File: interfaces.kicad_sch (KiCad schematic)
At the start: 126 parts, among them J6001 HDMI-A_WE_685119134923, J6002 USB-C_USB4105-GF-A, J6003 MicroSD_693071020811, Q6001 BSS138PW, Q6002 BSS138PW, Q6003 BSS138PW, Q6004 BSS138PW, Q6005 BSS138PW, Q6006 BSS138PW, Q6007 BSS138PW, Q6008 BSS138PW, SW6001 SW_KMR211NGLFS_SMD, U6001 FT4232H_VQFN, U6002 NCP718BSN330T1G, U6003 TXU0304BQAR, U6004 TPD4E05U06QDQARQ1, U6005 SN74HC595B, U6006 TPD4E05U06QDQARQ1, U6007 TPD4E05U06QDQARQ1, U6008 TXU0304BQAR, U6009 TPD4E05U06QDQARQ1, U6010 TPD4E05U06QDQARQ1, Y6001 Oscillator_SMD_12MHz_KX-7

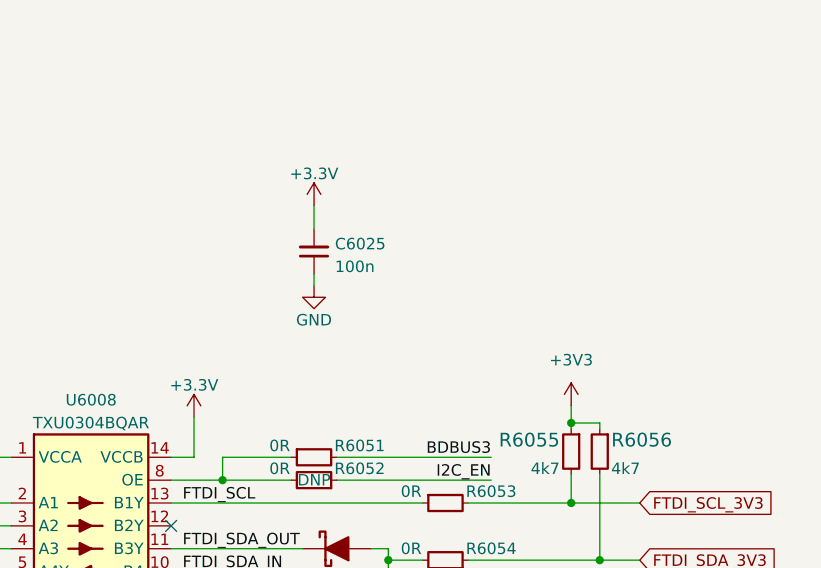
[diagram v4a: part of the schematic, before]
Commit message: Finish reworking power I2C and SPI termination
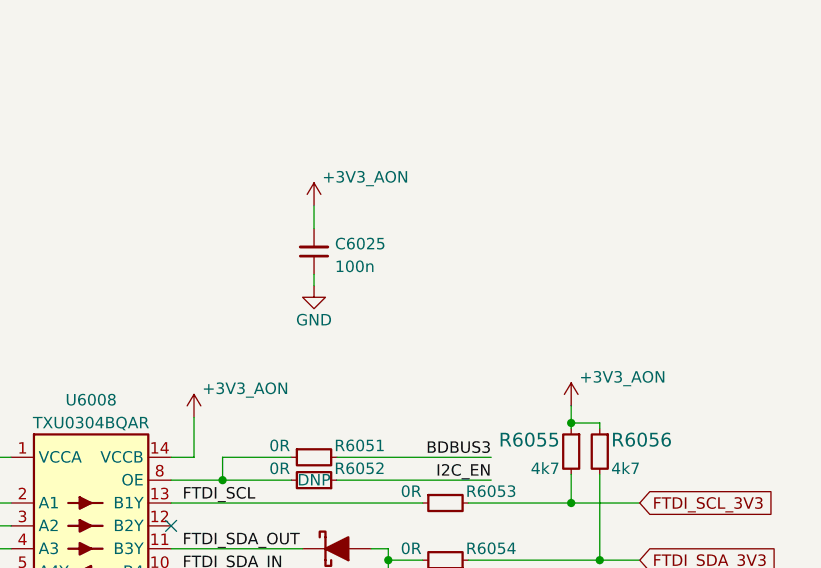
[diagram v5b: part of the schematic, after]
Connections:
- net +3V3: no longer C6025.2, R6055.1, R6056.1, U6008.14 (VCCB)
- new net +3V3_AON: C6025.2, R6055.1, R6056.1, U6008.14 (VCCB)
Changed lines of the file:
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@@
-    (pin "1")
-  )
-  (symbol (lib_id "antmicropower:+3.3V") (at 403.86 338.455 0) (unit 1)
-    (in_bom yes) (on_board yes)
-    (property "Reference" "#PWR0260" (id 0) (at 403.86 342.265 0)
-      (effects (font (size 1.27 1.27)) hide)
-    )
-    (property "Value" "+3.3V" (id 1) (at 403.86 334.899 0))
-    (property "Footprint" "" (id 2) (at 403.86 338.455 0)
-      (effects (font (size 1.27 1.27)) hide)
-    )
-    (property "Datasheet" "" (id 3) (at 403.86 338.455 0)
-      (effects (font (size 1.27 1.27)) hide)
-    )
     (pin "1")
   )
@@
     (pin "1")
     (pin "2")
+  )
+  (symbol (lib_id "sodimm-ddr5-tester:+3V3_AON") (at 417.195 314.96 0) (mirror y) (unit 1)
+    (in_bom yes) (on_board yes)
+    (property "Reference" "#PWR0260" (id 0) (at 417.195 318.77 0)
+      (effects (font (size 1.27 1.27)) hide)
+    )
+    (property "Value" "+3V3_AON" (id 1) (at 422.91 311.785 0))
+    (property "Footprint" "" (id 2) (at 417.195 314.96 0)
+      (effects (font (size 1.27 1.27)) hide)
+    )
+    (property "Datasheet" "" (id 3) (at 417.195 314.96 0)
+      (effects (font (size 1.27 1.27)) hide)
+    )
+    (pin "1")
   )
   (symbol (lib_id "sodimm-ddr5-tester:R_330R_0402") (at 177.8 238.125 270) (unit 1)
@@
     (pin "1")
     (pin "2")
+  )
+  (symbol (lib_id "sodimm-ddr5-tester:+3V3_AON") (at 403.86 338.455 0) (mirror y) (unit 1)
+    (in_bom yes) (on_board yes)
+    (property "Reference" "#PWR0287" (id 0) (at 403.86 342.265 0)
+      (effects (font (size 1.27 1.27)) hide)
+    )
+    (property "Value" "+3V3_AON" (id 1) (at 409.575 335.28 0))
+    (property "Footprint" "" (id 2) (at 403.86 338.455 0)
+      (effects (font (size 1.27 1.27)) hide)
+    )
+    (property "Datasheet" "" (id 3) (at 403.86 338.455 0)
+      (effects (font (size 1.27 1.27)) hide)
+    )
+    (pin "1")
+  )
+  (symbol (lib_id "sodimm-ddr5-tester:+3V3_AON") (at 445.77 337.185 0) (mirror y) (unit 1)
+    (in_bom yes) (on_board yes)
+    (property "Reference" "#PWR0265" (id 0) (at 445.77 340.995 0)
+      (effects (font (size 1.27 1.27)) hide)
+    )
+    (property "Value" "+3V3_AON" (id 1) (at 451.485 334.01 0))
+    (property "Footprint" "" (id 2) (at 445.77 337.185 0)
+      (effects (font (size 1.27 1.27)) hide)
+    )
+    (property "Datasheet" "" (id 3) (at 445.77 337.185 0)
+      (effects (font (size 1.27 1.27)) hide)
+    )
+    (pin "1")
   )
   (symbol (lib_id "sodimm-ddr5-tester:LED_RGY_0606_APTF1616SURKCGKSYKC") (at 152.4 229.87 0) (unit 1)
@@
     (pin "1")
   )
-  (symbol (lib_id "antmicropower:+3.3V") (at 417.195 314.96 0) (unit 1)
-    (in_bom yes) (on_board yes)
-    (property "Reference" "#PWR0287" (id 0) (at 417.195 318.77 0)
-      (effects (font (size 1.27 1.27)) hide)
-    )
-    (property "Value" "+3.3V" (id 1) (at 417.195 311.404 0))
-    (property "Footprint" "" (id 2) (at 417.195 314.96 0)
-      (effects (font (size 1.27 1.27)) hide)
-    )
-    (property "Datasheet" "" (id 3) (at 417.195 314.96 0)
-      (effects (font (size 1.27 1.27)) hide)
-    )
-    (pin "1")
-  )
   (symbol (lib_id "sodimm-ddr5-tester:R_330R_0402") (at 379.095 55.88 0) (unit 1)
     (in_bom yes) (on_board yes)
@@
     )
     (pin "1")
-  )
-  (symbol (lib_id "sodimm-ddr5-tester:+3V3") (at 445.77 337.185 0) (unit 1)
-    (in_bom yes) (on_board yes) (fields_autoplaced)
-    (property "Reference" "#PWR0265" (id 0) (at 445.77 340.995 0)
-      (effects (font (size 1.27 1.27)) hide)
-    )
-    (property "Value" "+3V3" (id 1) (at 445.77 332.105 0))
-    (property "Footprint" "" (id 2) (at 445.77 337.185 0)
-      (effects (font (size 1.27 1.27)) hide)
-    )
-    (property "Datasheet" "" (id 3) (at 445.77 337.185 0)
-      (effects (font (size 1.27 1.27)) hide)
-    )
-    (pin "1")

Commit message: SD card, flash, HDMI length matching and deskewing, add 0Ohm I2C mux bypass, Clean DRC, add DNP silkscreen marking, finish copper balancing
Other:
- moved on the sheet: C6018, C6019, C6021, C6022, C6023, C6024, C6025, D6008, D6009, D6010, D6011, D6012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
